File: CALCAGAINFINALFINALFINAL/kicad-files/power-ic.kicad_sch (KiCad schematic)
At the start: 19 parts, among them J2 USB_C_Receptacle_USB2.0_16P, J4 Conn_01x02, U5 TP4056-42-ESOP8, U6 TLV61070ADBV

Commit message: Turns out my whole power thing was absolutely retarded i should REALLY stop relying on gemini its actually retarded as fuh. Ima start js rawdogging it w forums and reddit. once its functional ima order it. i gota remember there no deadline better do it right the first time.
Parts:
- added U1: AP2112K-3.3, Package_TO_SOT_SMD:SOT-23-5, symbol Regulator_Linear:AP2112K-3.3
- J4: LCSC (none) -> C157931
- L2: footprint Inductor_SMD:L_6.3x6.3_H3 -> Inductor_SMD:L_0603_1608Metric; KiLib_Generator (none) -> SMD_2terminal_chip_molded
- R10, R11, R12, R13, R14, R8, R9: footprint Resistor_SMD:R_0201_0603Metric -> Resistor_SMD:R_0603_1608Metric
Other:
- note added: "to-do: 1.delete TLV 2. use LDO instead 3. check the data pinout/update yo excel sheet"
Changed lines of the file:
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@@
+		)
+	)
+	(text "to-do:\n1.delete TLV\n2. use LDO instead\n3. check the data pinout/update yo excel sheet\n"
+		(exclude_from_sim no)
+		(at 205.74 108.966 0)
+		(effects
+			(font
+				(size 1.27 1.27)
+			)
 		)
 	)
@@
 			)
 		)
-		(property "Footprint" "Resistor_SMD:R_0201_0603Metric"
+		(property "Footprint" "Resistor_SMD:R_0603_1608Metric"
 			(at 233.172 72.644 90)
 			(hide yes)
@@
 			)
 		)
-		(property "Description" "Resistor"
+		(property "Description" ""
 			(at 234.95 72.644 0)
 			(hide yes)
@@
 						(name "goody2shoes-nocamera")
 					)
+				)
+			)
+		)
+	)
+	(symbol
+		(lib_id "Regulator_Linear:AP2112K-3.3")
+		(at 176.53 97.79 0)
+		(unit 1)
+		(body_style 1)
+		(exclude_from_sim no)
+		(in_bom yes)
+		(on_board yes)
+		(in_pos_files yes)
+		(dnp no)
+		(fields_autoplaced yes)
+		(property "Reference" "U1"
+			(at 176.53 88.9 0)
+			(show_name no)
+			(do_not_autoplace no)
+			(effects
+				(font
+					(size 1.27 1.27)
+				)
+			)
+		)
+		(property "Value" "AP2112K-3.3"
+			(at 176.53 91.44 0)
+			(show_name no)
+			(do_not_autoplace no)
+			(effects
+				(font
+					(size 1.27 1.27)
+				)
+			)
+		)
+		(property "Footprint" "Package_TO_SOT_SMD:SOT-23-5"
+			(at 176.53 89.535 0)
+			(hide yes)
+			(show_name no)
+			(do_not_autoplace no)
+			(effects
+				(font
+					(size 1.27 1.27)
+				)
+			)
+		)
+		(property "Datasheet" "https://www.diodes.com/assets/Datasheets/AP2112.pdf"
+			(at 176.53 95.25 0)
+			(hide yes)
+			(show_name no)
+			(do_not_autoplace no)
+			(effects
+				(font
+					(size 1.27 1.27)
+				)
+			)
+		)
+		(property "Description" "600mA low dropout linear regulator, with enable pin, 3.8V-6V input voltage range, 3.3V fixed positive output, SOT-23-5"
+			(at 176.53 97.79 0)
+			(hide yes)
+			(show_name no)
+			(do_not_autoplace no)
+			(effects
+				(font
+					(size 1.27 1.27)
+				)
+			)
+		)
+		(pin "4"
+		)
+		(pin "3"
+		)
+		(pin "2"
+		)
+		(pin "1"
+		)
+		(pin "5"
+		)
+		(instances
+			(project "Cfx-port"
+				(path "/2a954a11-6412-4ea5-a14b-9a2b1d8affbf/37feafbc-0c2c-41fc-9817-e2aecf519d1e"
+					(reference "U1")
+					(unit 1)
 				)
 			)
@@
 			)
 		)
-		(property "Footprint" "Inductor_SMD:L_6.3x6.3_H3"
+		(property "Footprint" "Inductor_SMD:L_0603_1608Metric"
 			(at 219.456 55.118 0)
 			(hide yes)
@@
 			)
 		)
-		(property "Description" "Inductor"
+		(property "Description" ""
 			(at 219.456 55.118 0)
 			(hide yes)
@@
 		)
 		(property "LCSC" "C1035"
+			(at 219.456 55.118 0)
+			(hide yes)
+			(show_name no)
+			(do_not_autoplace no)
+			(effects
+				(font
+					(size 1.27 1.27)
+				)
+			)
+		)
+		(property "KiLib_Generator" "SMD_2terminal_chip_molded"
 			(at 219.456 55.118 0)
 			(hide yes)
@@
 			)
 		)
-		(property "Footprint" "Resistor_SMD:R_0201_0603Metric"
+		(property "Footprint" "Resistor_SMD:R_0603_1608Metric"
 			(at 227.584 84.836 90)
 			(hide yes)
@@
 			)
 		)
-		(property "Description" "Resistor"
+		(property "Description" ""
 			(at 229.362 84.836 0)
 			(hide yes)
@@
 			)
 		)
-		(property "Footprint" "Resistor_SMD:R_0201_0603Metric"
+		(property "Footprint" "Resistor_SMD:R_0603_1608Metric"
 			(at 82.296 69.088 90)
 			(hide yes)
@@
 			)
 		)
-		(property "Description" "Resistor"
+		(property "Description" ""
 			(at 82.296 67.31 0)
 			(hide yes)
@@
 			)
 		)
-		(property "Footprint" "Resistor_SMD:R_0201_0603Metric"
+		(property "Footprint" "Resistor_SMD:R_0603_1608Metric"
 			(at 144.272 76.962 90)
 			(hide yes)
@@
 			)
 		)
-		(property "Description" "Resistor"
+		(property "Description" ""
 			(at 144.272 75.184 0)
 			(hide yes)
@@
 			)
 		)
-		(property "Footprint" "Resistor_SMD:R_0201_0603Metric"
+		(property "Footprint" "Resistor_SMD:R_0603_1608Metric"
 			(at 82.296 71.628 90)
 			(hide yes)
@@
 			)
 		)
-		(property "Description" "Resistor"
+		(property "Description" ""
 			(at 82.296 69.85 0)
 			(hide yes)
@@
 			)
 		)
-		(property "Footprint" "Resistor_SMD:R_0201_0603Metric"
+		(property "Footprint" "Resistor_SMD:R_0603_1608Metric"
 			(at 174.752 76.962 90)
 			(hide yes)
@@
 			)
 		)
-		(property "Description" "Resistor"
+		(property "Description" ""
 			(at 174.752 75.184 0)
 			(hide yes)
@@
 			)
 		)
-		(property "Footprint" "Resistor_SMD:R_0201_0603Metric"
+		(property "Footprint" "Resistor_SMD:R_0603_1608Metric"
 			(at 144.272 74.422 90)
 			(hide yes)
@@
 			)
 		)
-		(property "Description" "Resistor"
+		(property "Description" ""
 			(at 144.272 72.644 0)
 			(hide yes)
@@
 			(at 195.326 42.164 0)
 			(hide yes)
+			(show_name no)
+			(do_not_autoplace no)
+			(effects
+				(font
+					(size 1.27 1.27)
+				)
+			)
+		)
+		(property "LCSC" "C157931"
+			(at 195.326 42.164 0)
+			(hide yes)

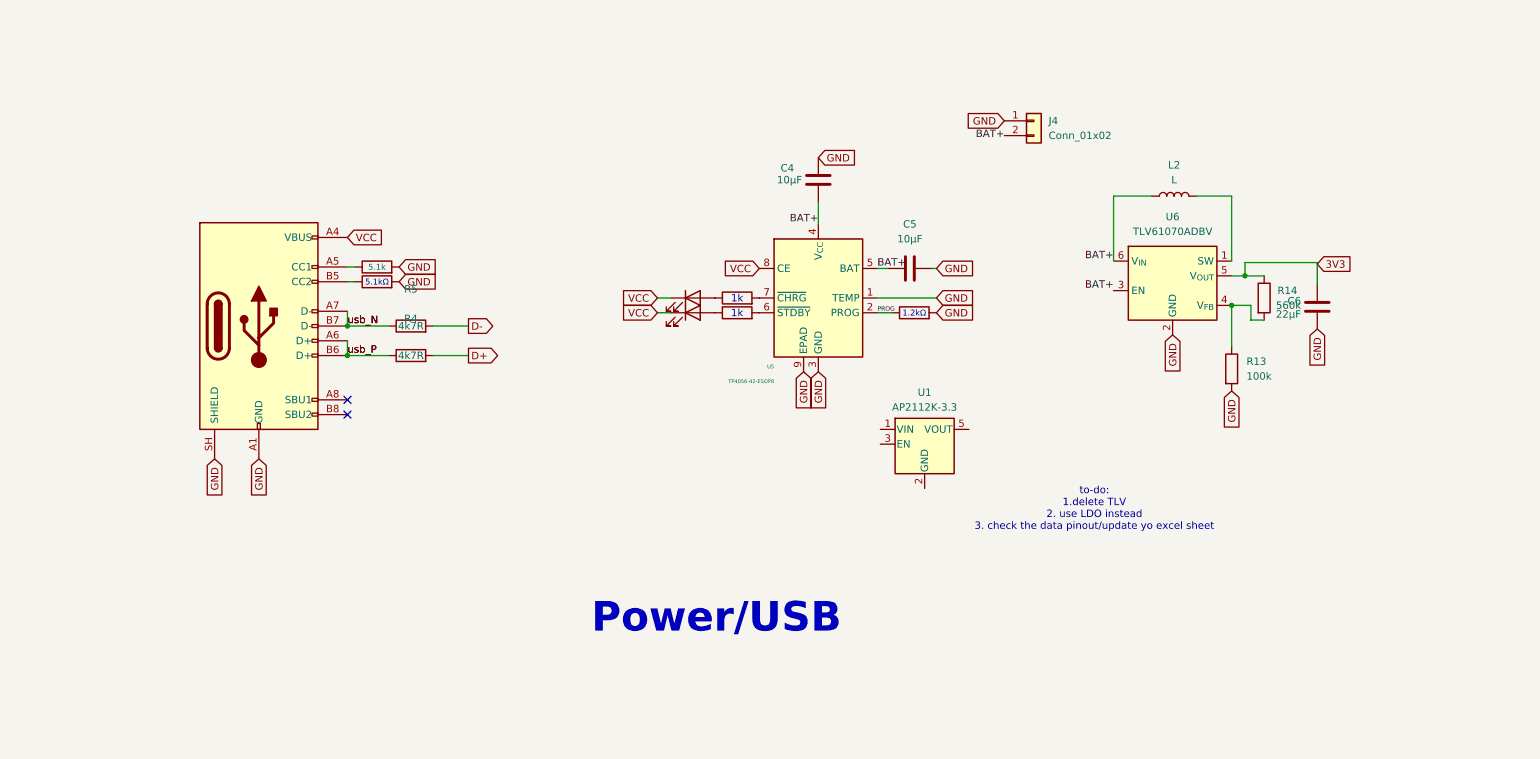
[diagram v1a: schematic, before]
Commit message: workin on matching up the pcb with the schematic gona chuck it on pcbreview then wait till i can stack up enough cash to order the first pcba. i need to make sure the design is 100% otherwise im js spending 300 bucks on a paperweight. so far the logic seems good js need to fix up some clerical errors w schematic.
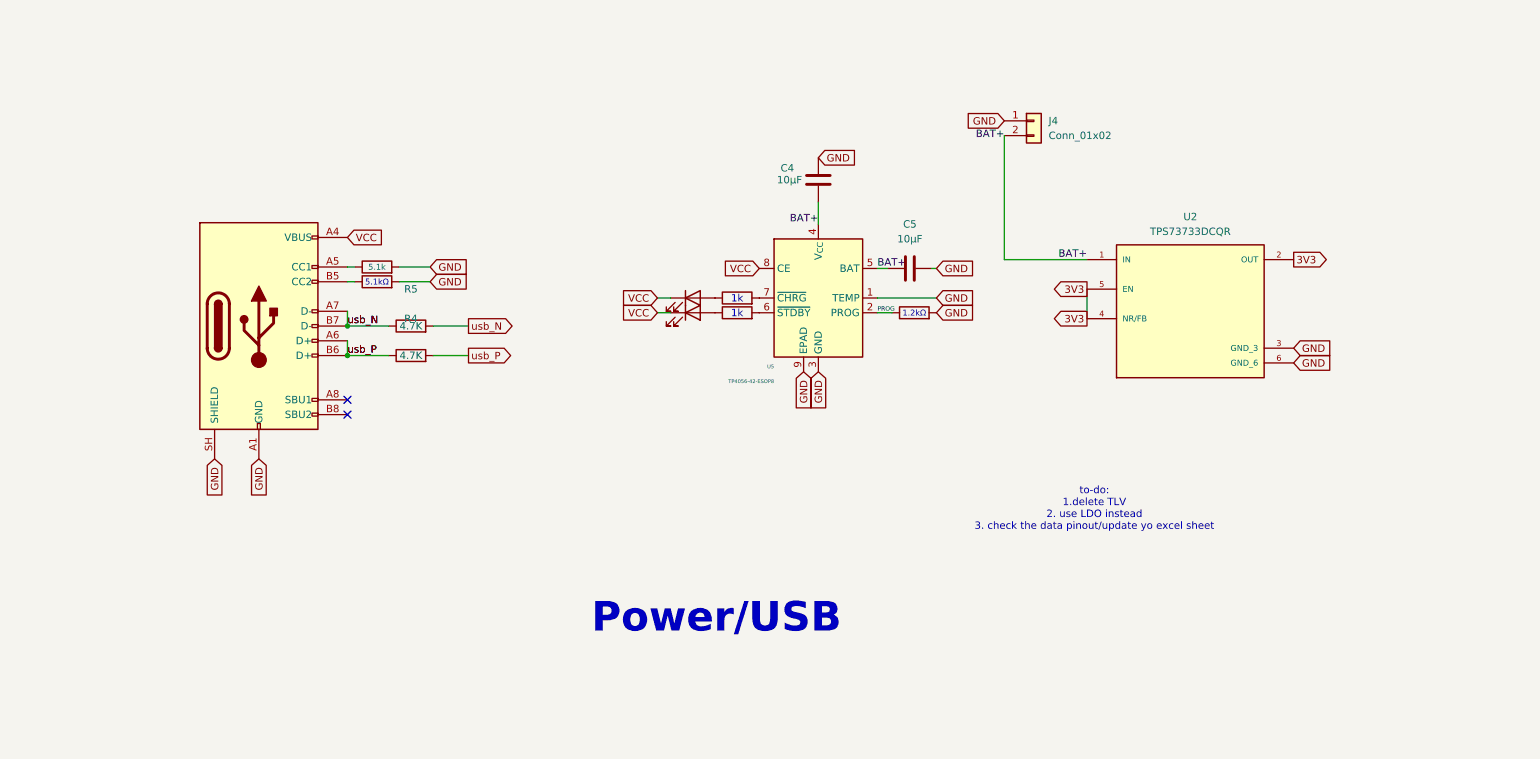
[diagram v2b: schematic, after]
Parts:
- removed C6: 22µF, Capacitor_SMD:C_0603_1608Metric, symbol Device:C
- removed L2: L, Inductor_SMD:L_0603_1608Metric, symbol Device:L
- removed R13: 100k, Resistor_SMD:R_0603_1608Metric, symbol Device:R
- removed R14: 560k, Resistor_SMD:R_0603_1608Metric, symbol Device:R
- removed U1: AP2112K-3.3, Package_TO_SOT_SMD:SOT-23-5, symbol Regulator_Linear:AP2112K-3.3
- removed U6: TLV61070ADBV, Package_TO_SOT_SMD:SOT-23-6, symbol Regulator_Switching:TLV61070ADBV
- added U2: TPS73733DCQR, TPS73733DCQR:IC_TPS73733DCQR, symbol New_Library:TPS73733DCQR
- R10, R11: value R -> 1k
- R4, R5: value 4k7R -> 4.7K
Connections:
- net D+ is gone; now on net usb_P: R4.2
- net D- is gone; now on net usb_N: R5.2
- net 3V3: now also U2.2 (OUT), U2.4 (NR/FB), U2.5 (EN)
- net BAT+: now also U2.1 (IN)
- net GND: now also U2.3 (GND_3), U2.6 (GND_6)

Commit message: yo chat this actually for reals the order now im ordering it and neva openin kicad again ong
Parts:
- removed R4, R5: 4.7K, symbol Device:R
- added D8: 1N5819, Diode_THT:D_DO-41_SOD81_P10.16mm_Horizontal, symbol Diode:1N5819
- added Q1: DMP3099L, Package_TO_SOT_SMD:SOT-23, symbol Transistor_FET:DMP3099L
- added R15, R16, R17: 100k, symbol Device:R
- C4: value 10µF -> 1uf; footprint Capacitor_SMD:C_0603_1608Metric -> (none); KiLib_Generator SMD_2terminal_chip_molded -> (none); LCSC C7171 -> (none)
- renumbered U2 to LDO1
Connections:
- net 3V3: no longer LDO1.4 (NR/FB), LDO1.5 (EN)
- net BAT+: now also Q1.2 (S); no longer C4.2, LDO1.1 (IN), U5.4 (V_{CC})
- net GND: now also C4.2, R17.2; no longer C4.1
- net VCC: now also U5.4 (V_{CC}), D8.2 (A), Q1.1 (G), R17.1
- new net: R15.1, R16.2
- new net: C4.1, D8.1 (K), LDO1.1 (IN), LDO1.4 (NR/FB), LDO1.5 (EN), Q1.3 (D)
- new net batprog: R15.2, R16.1
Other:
- note added: "JST connector"
- note added: "baloney"
- moved on the sheet: C5, LDO1, U5
